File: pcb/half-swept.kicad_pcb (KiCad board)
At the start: 2 copper layers, 108.6 x 86.9 mm, 23 parts, among them J1 AudioJack4dpb, J2 AudioJack4dpb, SW1 SW_Push, SW10 SW_Push, SW11 SW_Push, SW12 SW_Push, SW14 SW_Push, SW15 SW_Push, SW16 SW_Push, SW17 SW_Push, SW18 SW_Push, SW2 SW_Push, SW20 SW_Push, SW21 SW_Push, SW3 SW_Push, SW4 SW_Push, SW5 SW_Push, SW6 SW_Push, SW8 SW_Push, SW9 SW_Push, U2 Elite-C

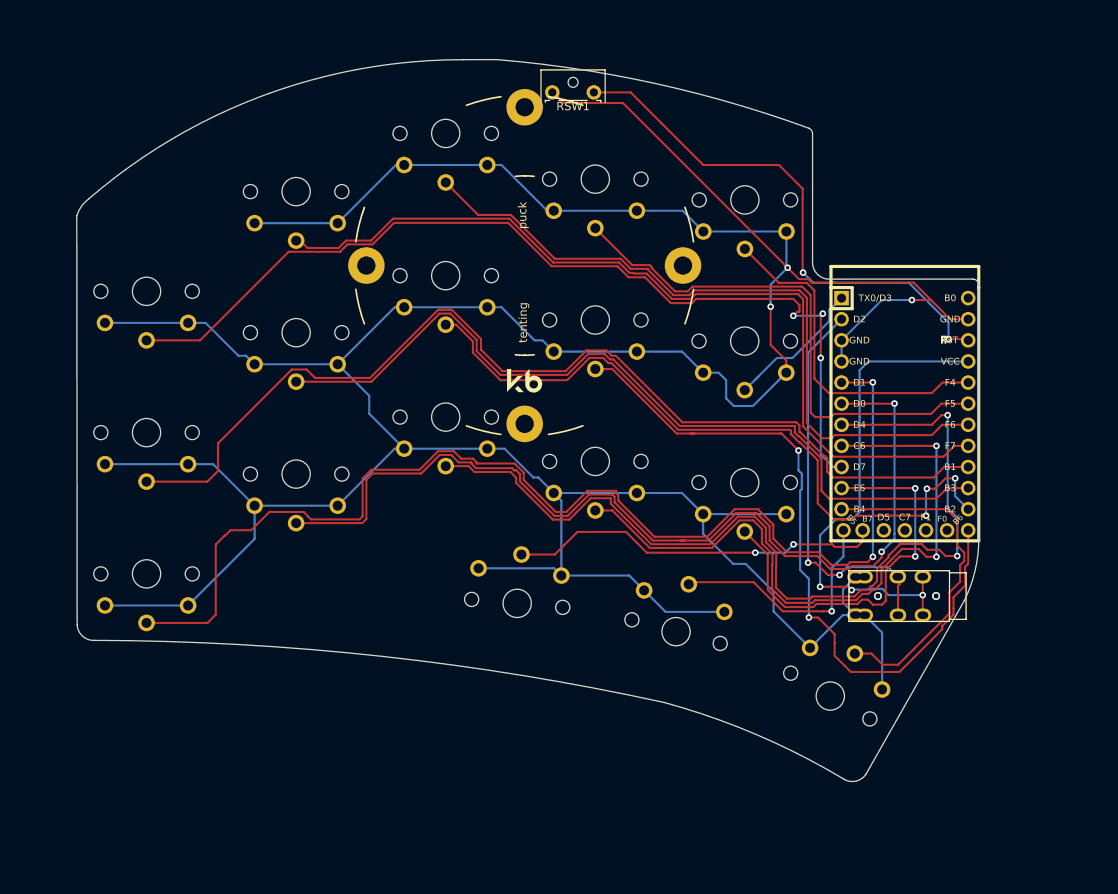
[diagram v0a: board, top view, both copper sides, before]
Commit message: updated to include per key led support, oled support, 36 keys, still needs routing
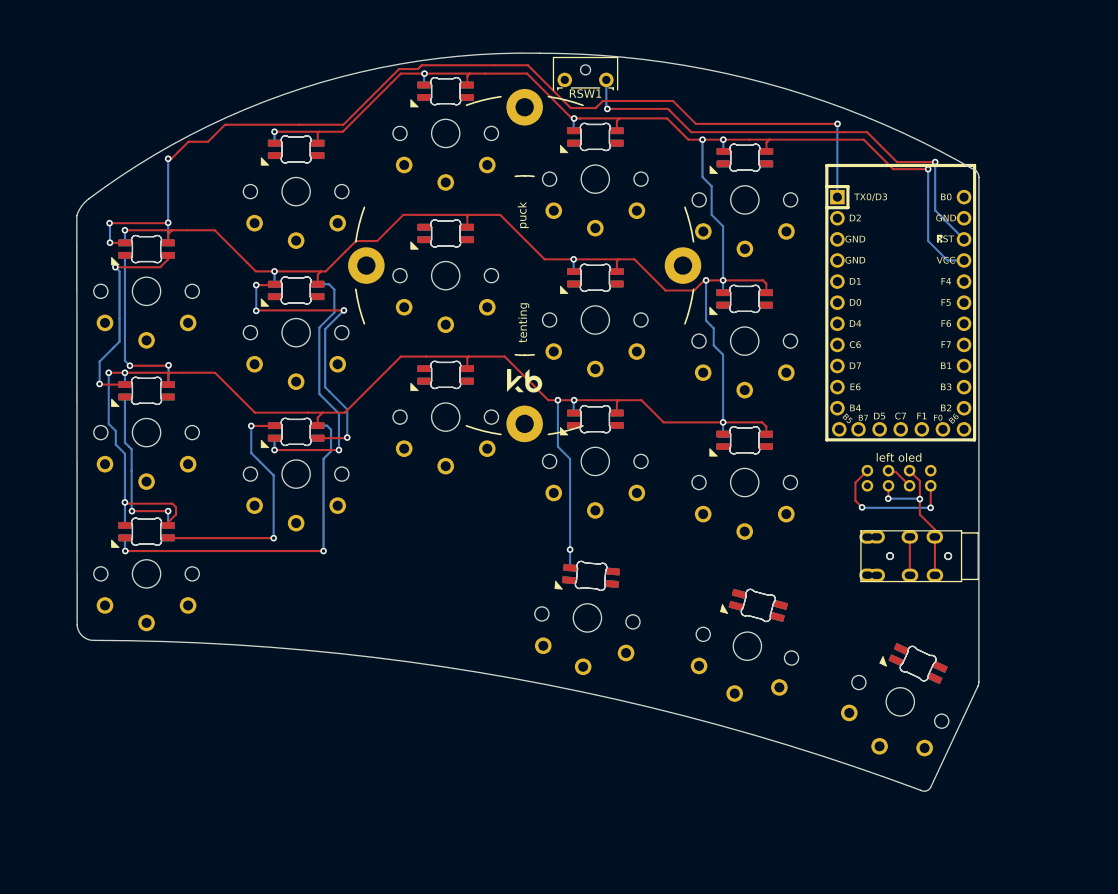
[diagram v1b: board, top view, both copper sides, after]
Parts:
- added D1: SK6812MINI-E, sweep36:MX_SK6812MINI-E_REV, F.Cu at (22.0, 41.0)
- added D10: SK6812MINI-E, sweep36:MX_SK6812MINI-E_REV, F.Cu at (40.0, 63.0)
- added D11: SK6812MINI-E, sweep36:MX_SK6812MINI-E_REV, F.Cu at (76.0, 61.5)
- added D12: SK6812MINI-E, sweep36:MX_SK6812MINI-E_REV, F.Cu at (75.0, 80.3)
- added D13: SK6812MINI-E, sweep36:MX_SK6812MINI-E_REV, F.Cu at (40.0, 46.0)
- added D14: SK6812MINI-E, sweep36:MX_SK6812MINI-E_REV, F.Cu at (76.0, 44.5)
- added D15: SK6812MINI-E, sweep36:MX_SK6812MINI-E_REV, F.Cu at (94.3, 83.7)
- added D16: SK6812MINI-E, sweep36:MX_SK6812MINI-E_REV, F.Cu at (40.0, 29.0)
- added D17: SK6812MINI-E, sweep36:MX_SK6812MINI-E_REV, F.Cu at (76.0, 27.5)
- added D18: SK6812MINI-E, sweep36:MX_SK6812MINI-E_REV, F.Cu at (112.7, 90.4)
- added D19: SK6812MINI-E, sweep36:MX_SK6812MINI-E_REV, B.Cu at (22.0, 41.0)
- added D2: SK6812MINI-E, sweep36:MX_SK6812MINI-E_REV, F.Cu at (58.0, 22.0)
- added D20: SK6812MINI-E, sweep36:MX_SK6812MINI-E_REV, B.Cu at (58.0, 22.0)
- added D21: SK6812MINI-E, sweep36:MX_SK6812MINI-E_REV, B.Cu at (94.0, 30.0)
- added D22: SK6812MINI-E, sweep36:MX_SK6812MINI-E_REV, B.Cu at (22.0, 58.0)
- added D23: SK6812MINI-E, sweep36:MX_SK6812MINI-E_REV, B.Cu at (58.0, 39.1)
- added D24: SK6812MINI-E, sweep36:MX_SK6812MINI-E_REV, B.Cu at (94.0, 47.0)
- added D25: SK6812MINI-E, sweep36:MX_SK6812MINI-E_REV, B.Cu at (22.0, 75.0)
- added D26: SK6812MINI-E, sweep36:MX_SK6812MINI-E_REV, B.Cu at (58.0, 56.1)
- added D27: SK6812MINI-E, sweep36:MX_SK6812MINI-E_REV, B.Cu at (94.0, 64.0)
- added D28: SK6812MINI-E, sweep36:MX_SK6812MINI-E_REV, B.Cu at (40.0, 63.0)
- added D29: SK6812MINI-E, sweep36:MX_SK6812MINI-E_REV, B.Cu at (76.0, 61.5)
- added D3: SK6812MINI-E, sweep36:MX_SK6812MINI-E_REV, F.Cu at (94.0, 30.0)
- added D30: SK6812MINI-E, sweep36:MX_SK6812MINI-E_REV, B.Cu at (75.0, 80.3)
- added D31: SK6812MINI-E, sweep36:MX_SK6812MINI-E_REV, B.Cu at (40.0, 46.0)
- added D32: SK6812MINI-E, sweep36:MX_SK6812MINI-E_REV, B.Cu at (76.0, 44.5)
- added D33: SK6812MINI-E, sweep36:MX_SK6812MINI-E_REV, B.Cu at (94.3, 83.7)
- added D34: SK6812MINI-E, sweep36:MX_SK6812MINI-E_REV, B.Cu at (40.0, 29.0)
- added D35: SK6812MINI-E, sweep36:MX_SK6812MINI-E_REV, B.Cu at (76.0, 27.5)
- added D36: SK6812MINI-E, sweep36:MX_SK6812MINI-E_REV, B.Cu at (112.7, 90.4)
- added D4: SK6812MINI-E, sweep36:MX_SK6812MINI-E_REV, F.Cu at (22.0, 58.0)
- added D5: SK6812MINI-E, sweep36:MX_SK6812MINI-E_REV, F.Cu at (58.0, 39.1)
- added D6: SK6812MINI-E, sweep36:MX_SK6812MINI-E_REV, F.Cu at (94.0, 47.0)
- added D7: SK6812MINI-E, sweep36:MX_SK6812MINI-E_REV, F.Cu at (22.0, 75.0)
- added D8: SK6812MINI-E, sweep36:MX_SK6812MINI-E_REV, F.Cu at (58.0, 56.1)
- added D9: SK6812MINI-E, sweep36:MX_SK6812MINI-E_REV, F.Cu at (94.0, 64.0)
- added OL1: OLED, sweep36:OLED_v2, F.Cu at (112.5, 62.6)
- added OL2: OLED, sweep36:OLED_v2, B.Cu at (112.5, 64.4)
- moved U2 12.2 mm to (112.8, 43.6)
- moved SW21 8.76 mm to (94.3, 83.7), turned to -15 degrees
- moved SW1 8.63 mm to (75.0, 80.3), turned to -5 degrees
- moved SW20 8.45 mm to (112.7, 90.4), turned to -25 degrees
- moved J1 5.01 mm to (120.0, 72.8)
- moved J2 5.01 mm to (120.1, 72.9)
- moved RSW1 2.12 mm to (72.3, 15.6)
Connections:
- U2 pad 1: Switch10 -> led
- U2 pad 26: unconnected-(U2-Pad26) -> Switch10
- U2 pad 27: unconnected-(U2-Pad27) -> Switch11
- U2 pad 28: unconnected-(U2-Pad28) -> Switch12
- U2 pad 5: Switch11 -> sda
- U2 pad 6: Switch12 -> scl
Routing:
- net gnd: track 476.5 -> 0.00 mm, vias 3 -> 0
- net vcc: track 60.3 -> 415.3 mm, vias 3 -> 20
- net Switch11: track 142.2 -> 0.00 mm, vias 2 -> 0
- net Switch6: track 123.3 -> 0.00 mm
- net led: track 0.00 -> 119.0 mm, vias 0 -> 5
- net Switch12: track 115.8 -> 0.00 mm, vias 2 -> 0
- net Switch1: track 114.5 -> 0.00 mm, vias 3 -> 0
- net Switch13: track 112.3 -> 0.00 mm, vias 2 -> 0
- net Switch2: track 104.5 -> 0.00 mm
- net Switch7: track 99.6 -> 0.00 mm
- net Switch9: track 86.9 -> 0.00 mm, vias 2 -> 0
- net Switch3: track 85.9 -> 0.00 mm
- net Switch8: track 85.7 -> 0.00 mm, vias 3 -> 0
- net Switch14: track 81.2 -> 0.00 mm, vias 2 -> 0
- net Switch4: track 63.8 -> 0.00 mm
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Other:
- board size 108.6 x 86.9 mm -> 108.6 x 88.8 mm

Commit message: finished routing to complete elite-c, oled, per key led, and 36 key support
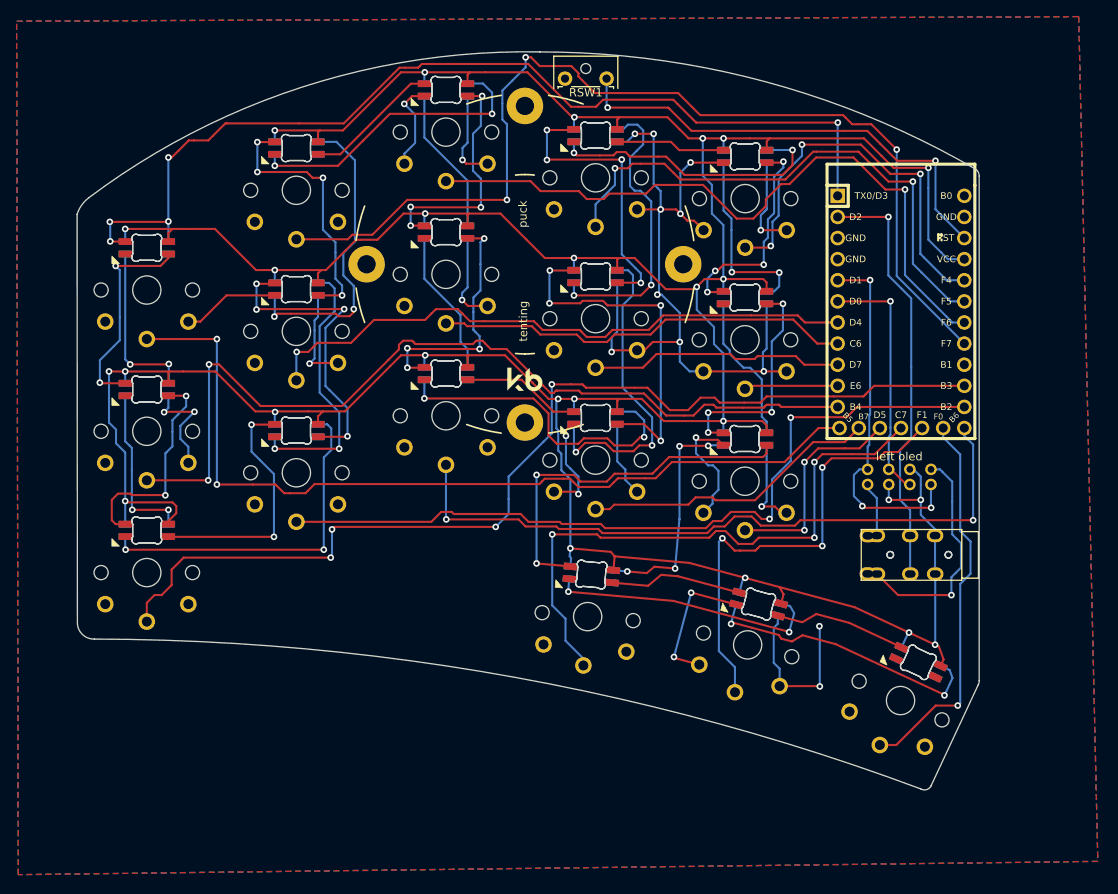
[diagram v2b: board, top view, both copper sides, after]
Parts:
- moved D18 0.16 mm to (112.7, 90.2)
- moved D36 0.16 mm to (112.7, 90.2)
- moved SW20 0.16 mm to (112.7, 90.2)
- moved D12 0.16 mm to (75.1, 80.1)
- moved D30 0.16 mm to (75.1, 80.1)
- moved J2 0.16 mm to (120.1, 72.7)
- moved SW1 0.16 mm to (75.1, 80.1)
- moved D15 0.16 mm to (94.3, 83.5)
- moved D33 0.16 mm to (94.3, 83.5)
- moved SW21 0.16 mm to (94.3, 83.5)
- moved D17 0.16 mm to (76.0, 27.3)
- moved D25 0.16 mm to (22.0, 74.8)
- moved D35 0.16 mm to (76.0, 27.3)
- moved D7 0.16 mm to (22.0, 74.8)
- moved OL2 0.16 mm to (112.6, 64.2)
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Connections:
- U2 pad 10: Switch15 -> Switch10
- U2 pad 11: Switch16 -> Switch6
- U2 pad 12: Switch17 -> Switch1
- U2 pad 13: Switch9 -> Switch13
- U2 pad 14: Switch8 -> Switch12
- U2 pad 15: Switch7 -> Switch11
- U2 pad 16: Switch6 -> unconnected-(U2-Pad16)
- U2 pad 25: Switch18 -> Switch14
- U2 pad 26: Switch10 -> Switch15
- U2 pad 27: Switch11 -> Switch18
- U2 pad 28: Switch12 -> Switch17
- U2 pad 29: unconnected-(U2-Pad29) -> Switch16
- U2 pad 7: Switch13 -> Switch7
- U2 pad 8: Switch14 -> Switch8
- U2 pad 9: Switch1 -> Switch9
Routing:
- net gnd: track 0.00 -> 294.4 mm, vias 0 -> 25
- net Switch11: track 0.00 -> 123.6 mm, vias 0 -> 4
- net Switch2: track 0.00 -> 122.0 mm, vias 0 -> 3
- net Switch6: track 0.00 -> 107.9 mm, vias 0 -> 2
- net Switch1: track 0.00 -> 105.4 mm, vias 0 -> 2
- net Switch12: track 0.00 -> 94.1 mm, vias 0 -> 2
- net Switch13: track 0.00 -> 83.8 mm, vias 0 -> 2
- net Switch3: track 0.00 -> 83.4 mm, vias 0 -> 1
- net Switch7: track 0.00 -> 73.5 mm, vias 0 -> 1
- net Switch18: track 0.00 -> 71.5 mm, vias 0 -> 3
- net vcc: track 415.3 -> 485.5 mm, vias 20 -> 26
- net Switch4: track 0.00 -> 65.7 mm, vias 0 -> 2
- net Switch17: track 0.00 -> 56.0 mm, vias 0 -> 3
- net Switch8: track 0.00 -> 50.4 mm
- net Switch5: track 0.00 -> 49.0 mm, vias 0 -> 3
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- added copper zone on B.Cu, net gnd
- added copper zone on F.Cu, net gnd

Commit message: converted to choc reversible hotswap
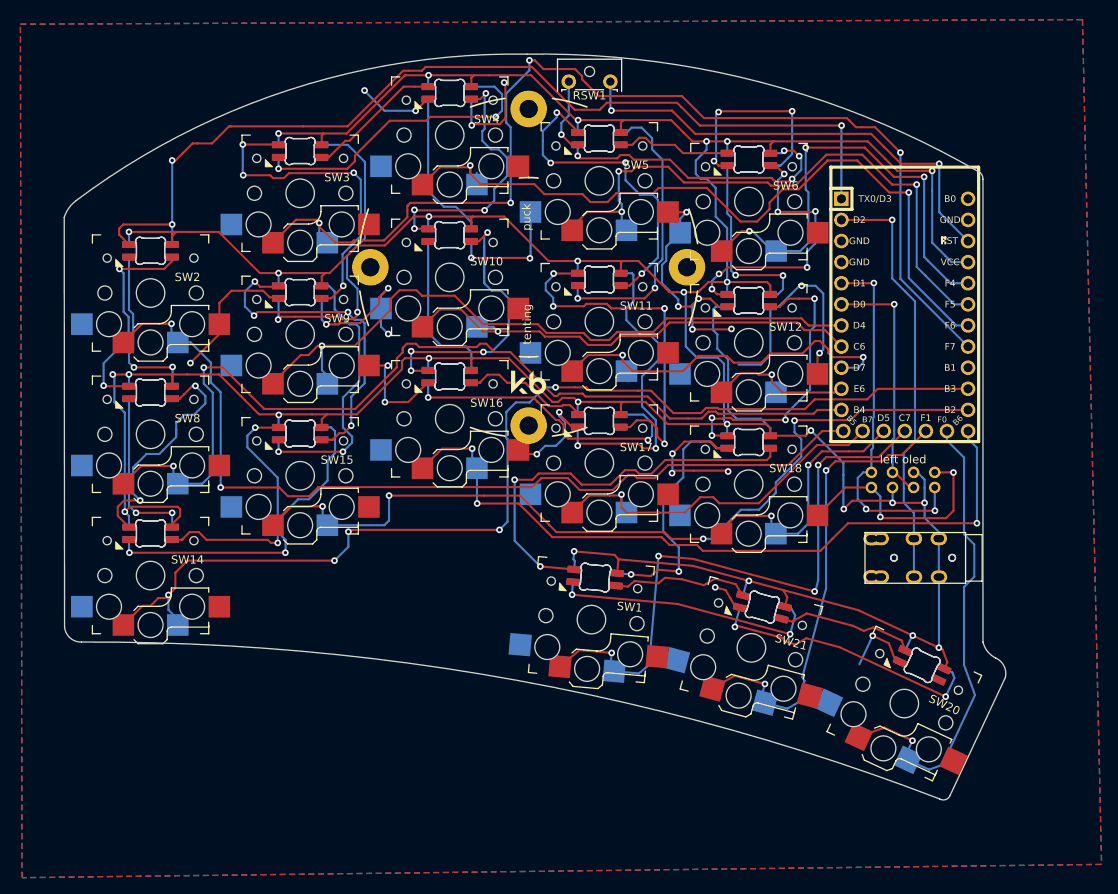
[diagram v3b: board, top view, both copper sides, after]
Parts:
- SW1, SW10, SW11, SW12, SW14, SW15, SW16, SW17, SW18, SW2, SW20, SW21, SW3, SW4, SW5, SW6, SW8, SW9: footprint Keebio-Parts:Kailh-PG1350-1u-reversible -> keyswitches:Kailh_socket_PG1350_reversible
- moved D14 0.58 mm to (76.5, 44.7)
- moved D32 0.58 mm to (76.5, 44.7)
- moved SW11 0.58 mm to (76.5, 44.7)
- moved D16 0.58 mm to (40.5, 29.2)
- moved D34 0.58 mm to (40.5, 29.2)
- moved SW3 0.58 mm to (40.5, 29.2)
- moved D27 0.58 mm to (94.5, 64.2)
- moved D9 0.58 mm to (94.5, 64.2)
- moved REF** 0.58 mm to (68.0, 38.1)
- moved J1 0.58 mm to (120.5, 73.1)
- moved D23 0.58 mm to (58.5, 39.3)
- moved D5 0.58 mm to (58.5, 39.3)
- moved SW10 0.58 mm to (58.5, 39.3)
- moved D11 0.58 mm to (76.5, 61.7)
- moved D29 0.58 mm to (76.5, 61.7)
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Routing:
- net gnd: track 294.4 -> 249.3 mm, vias 25 -> 32
- net Switch9: track 30.6 -> 46.0 mm, vias 0 -> 2
- net Switch16: track 46.7 -> 57.2 mm
- net Switch2: track 122.0 -> 131.4 mm, vias 3 -> 4
- net Switch7: track 73.5 -> 82.7 mm
- net Net-(D23-Pad2): track 29.3 -> 38.4 mm
- net vcc: track 485.5 -> 494.5 mm, vias 26 -> 27
- net Switch14: track 36.0 -> 44.7 mm, vias 0 -> 1
- net Switch12: track 94.1 -> 102.8 mm, vias 2 -> 4
- net Switch3: track 83.4 -> 91.9 mm, vias 1 -> 2
- net Switch10: track 11.3 -> 19.4 mm, vias 0 -> 1
- net Net-(D31-Pad2): track 31.9 -> 39.9 mm
- net Switch8: track 50.4 -> 58.1 mm, vias 0 -> 1
- net Net-(D21-Pad2): track 26.5 -> 34.0 mm, vias 4 -> 6
- net Switch5: track 49.0 -> 56.3 mm
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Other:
- board size 108.6 x 88.8 mm -> 113.3 x 89.7 mm
